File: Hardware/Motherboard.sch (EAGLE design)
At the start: 69 parts, among them J1 MICROMOD-2222-C, J10 MICRO-SD-PUSH-PUSH-EXT-PIN, J2 Vertical Qwiic Connector, J4 QWIIC_RIGHT_ANGLE, J5 CORTEX_JTAG_DEBUG_MINIMUM_PTH, J6 MICROMOD_CARRIER, J7 MICROMOD_CARRIER, Q1 3.1A/30V/105mΩ, U2 MCP73831, U5 AP7361C-33

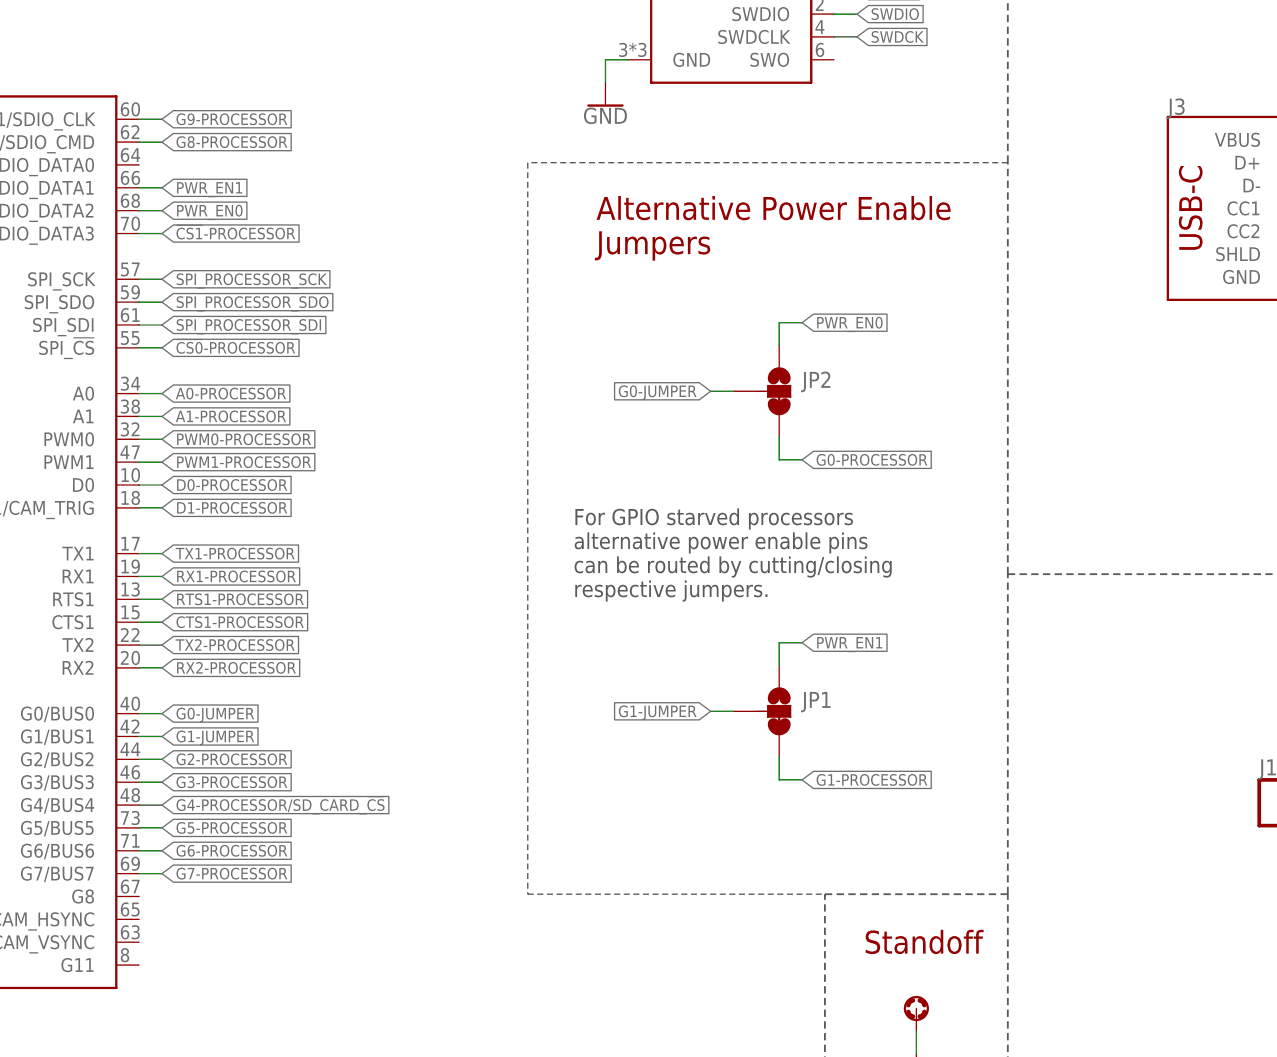
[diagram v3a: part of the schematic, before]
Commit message: Recreates changes from last change but instead moves jumpers to nets G5/G6
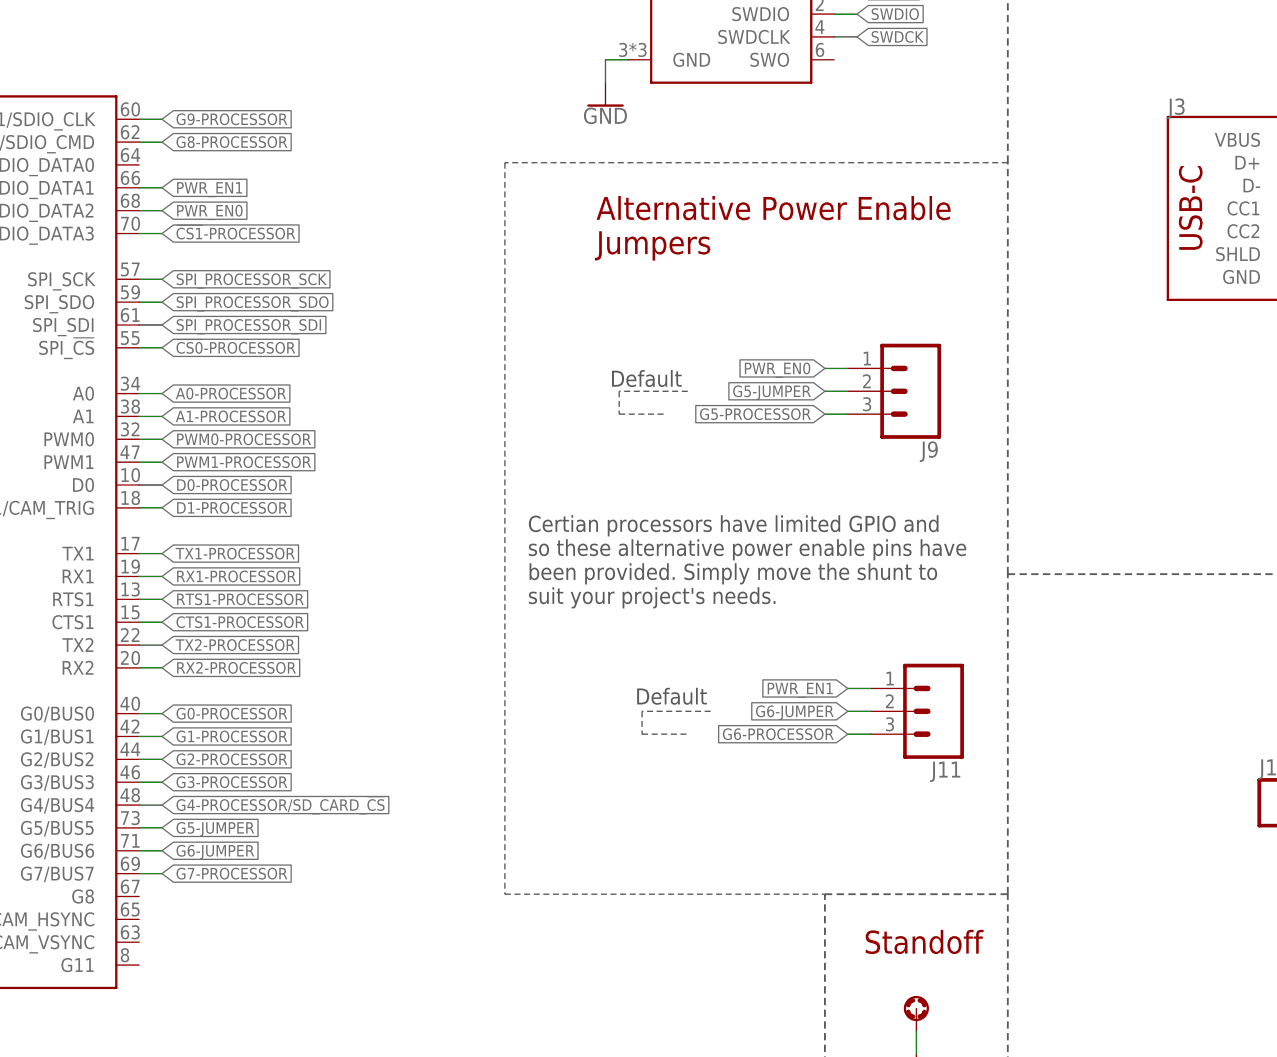
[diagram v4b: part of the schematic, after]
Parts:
- removed JP1, JP2: JUMPER-SMT_3_1-NC_TRACE_SILK, SparkFun-Jumpers:JUMPER-SMT_3_1-NC_TRACE_SILK
- added J11, J9: (no value), SparkFun-Connectors:CONN_03LOCK
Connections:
- removed net G0-JUMPER: J1.G0/BUS0, JP2.2
- removed net G1-JUMPER: J1.G1/BUS1, JP1.2
- new net G5-JUMPER: J1.G5/BUS5, J9.2
- new net G6-JUMPER: J1.G6/BUS6, J11.2
- net G0-PROCESSOR: now also J1.G0/BUS0; no longer JP2.3
- net G1-PROCESSOR: now also J1.G1/BUS1; no longer JP1.3
- net G5-PROCESSOR: now also J9.3; no longer J1.G5/BUS5
- net G6-PROCESSOR: now also J11.3; no longer J1.G6/BUS6
- net PWR_EN0: now also J9.1; no longer JP2.1
- net PWR_EN1: now also J11.1; no longer JP1.1
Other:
- note added: "Certian processors have limited GPIO and so these alternative power enable pins have been provided. Simply move the shunt to suit your project's needs."
- note added: "Default"
- note removed: "For GPIO starved processors alternative power enable pins can be routed by cutting/closing respective jumpers."
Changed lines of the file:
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@@
 <part name="R6" library="SparkFun-Resistors" deviceset="10KOHM" device="-0603-1/10W-1%" value="10k"/>
 <part name="GND8" library="SparkFun-PowerSymbols" deviceset="GND" device=""/>
-<part name="JP1" library="SparkFun-Jumpers" deviceset="JUMPER-SMT_3_1-NC_TRACE" device="_SILK" package3d_urn="urn:adsk.eagle:package:39288/1"/>
-<part name="JP2" library="SparkFun-Jumpers" deviceset="JUMPER-SMT_3_1-NC_TRACE" device="_SILK" package3d_urn="urn:adsk.eagle:package:39288/1"/>
+<part name="J9" library="SparkFun-Connectors" deviceset="CONN_03" device="LOCK"/>
+<part name="J11" library="SparkFun-Connectors" deviceset="CONN_03" device="LOCK"/>
 </parts>
 <sheets>
@@
 <text x="171.958" y="153.416" size="2.54" layer="94" font="vector">Standoff</text>
 <text x="187.96" y="22.86" size="2.54" layer="94" font="vector">Standoff</text>
-<wire x1="187.96" y1="241.3" x2="134.62" y2="241.3" width="0.1524" layer="97" style="longdash"/>
-<wire x1="134.62" y1="241.3" x2="134.62" y2="160.02" width="0.1524" layer="97" style="longdash"/>
-<wire x1="134.62" y1="160.02" x2="167.64" y2="160.02" width="0.1524" layer="97" style="longdash"/>
+<wire x1="187.96" y1="241.3" x2="132.08" y2="241.3" width="0.1524" layer="97" style="longdash"/>
+<wire x1="132.08" y1="241.3" x2="132.08" y2="160.02" width="0.1524" layer="97" style="longdash"/>
+<wire x1="132.08" y1="160.02" x2="167.64" y2="160.02" width="0.1524" layer="97" style="longdash"/>
 <text x="142.24" y="231.14" size="2.54" layer="94" font="vector">Alternative Power Enable
 Jumpers</text>
-<text x="139.7" y="193.04" size="1.778" layer="97" font="vector">For GPIO starved processors
-alternative power enable pins
-can be routed by cutting/closing
-respective jumpers.</text>
+<text x="134.62" y="192.278" size="1.778" layer="97" font="vector">Certian processors have limited GPIO and
+so these alternative power enable pins have
+been provided. Simply move the shunt to
+suit your project's needs.
+</text>
+<wire x1="154.94" y1="180.34" x2="147.32" y2="180.34" width="0.1524" layer="97" style="dashdot"/>
+<wire x1="147.32" y1="180.34" x2="147.32" y2="177.8" width="0.1524" layer="97" style="dashdot"/>
+<wire x1="147.32" y1="177.8" x2="152.4" y2="177.8" width="0.1524" layer="97" style="dashdot"/>
+<wire x1="152.4" y1="215.9" x2="144.78" y2="215.9" width="0.1524" layer="97" style="dashdot"/>
+<wire x1="144.78" y1="215.9" x2="144.78" y2="213.36" width="0.1524" layer="97" style="dashdot"/>
+<wire x1="144.78" y1="213.36" x2="149.86" y2="213.36" width="0.1524" layer="97" style="dashdot"/>
+<text x="143.764" y="216.408" size="1.778" layer="97" font="vector">Default</text>
+<text x="146.558" y="181.102" size="1.778" layer="97" font="vector">Default</text>
 </plain>
 <instances>
@@
 <attribute name="VALUE" x="264.16" y="218.186" size="1.778" layer="96" font="vector" align="top-center"/>
 </instance>
-<instance part="JP1" gate="G$1" x="162.56" y="180.34" smashed="yes">
-<attribute name="NAME" x="165.1" y="180.721" size="1.778" layer="95" font="vector"/>
-</instance>
-<instance part="JP2" gate="G$1" x="162.56" y="215.9" smashed="yes">
-<attribute name="NAME" x="165.1" y="216.281" size="1.778" layer="95" font="vector"/>
+<instance part="J9" gate="J$1" x="177.8" y="215.9" smashed="yes" rot="R180">
+<attribute name="VALUE" x="180.34" y="223.266" size="1.778" layer="96" font="vector" rot="R180"/>
+<attribute name="NAME" x="180.34" y="210.312" size="1.778" layer="95" font="vector" rot="R180"/>
+</instance>
+<instance part="J11" gate="J$1" x="180.34" y="180.34" smashed="yes" rot="R180">
+<attribute name="VALUE" x="182.88" y="187.706" size="1.778" layer="96" font="vector" rot="R180"/>
+<attribute name="NAME" x="182.88" y="174.752" size="1.778" layer="95" font="vector" rot="R180"/>
 </instance>
 </instances>
@@
 </segment>
 <segment>
-<pinref part="JP2" gate="G$1" pin="1"/>
-<wire x1="162.56" y1="220.98" x2="162.56" y2="223.52" width="0.1524" layer="91"/>
-<wire x1="162.56" y1="223.52" x2="165.1" y2="223.52" width="0.1524" layer="91"/>
-<label x="165.1" y="223.52" size="1.27" layer="95" font="vector" xref="yes"/>
+<label x="167.64" y="218.44" size="1.27" layer="95" font="vector" rot="R180" xref="yes"/>
+<pinref part="J9" gate="J$1" pin="1"/>
+<wire x1="170.18" y1="218.44" x2="167.64" y2="218.44" width="0.1524" layer="91"/>
 </segment>
 </net>
@@
 </segment>
 <segment>
-<pinref part="JP1" gate="G$1" pin="1"/>
-<wire x1="162.56" y1="185.42" x2="162.56" y2="187.96" width="0.1524" layer="91"/>
-<wire x1="162.56" y1="187.96" x2="165.1" y2="187.96" width="0.1524" layer="91"/>
-<label x="165.1" y="187.96" size="1.27" layer="95" font="vector" xref="yes"/>
+<label x="170.18" y="182.88" size="1.27" layer="95" font="vector" rot="R180" xref="yes"/>
+<pinref part="J11" gate="J$1" pin="1"/>
+<wire x1="172.72" y1="182.88" x2="170.18" y2="182.88" width="0.1524" layer="91"/>
 </segment>
 </net>
@@
 </segment>
 <segment>
-<pinref part="JP2" gate="G$1" pin="3"/>
-<wire x1="162.56" y1="210.82" x2="162.56" y2="208.28" width="0.1524" layer="91"/>
-<wire x1="162.56" y1="208.28" x2="165.1" y2="208.28" width="0.1524" layer="91"/>
-<label x="165.1" y="208.28" size="1.27" layer="95" font="vector" xref="yes"/>
+<pinref part="J1" gate="J1" pin="G0/BUS0"/>
+<wire x1="93.98" y1="180.086" x2="91.44" y2="180.086" width="0.1524" layer="91"/>
+<label x="93.98" y="180.086" size="1.27" layer="95" font="vector" xref="yes"/>
 </segment>
 </net>
@@
 </segment>
 <segment>
-<pinref part="JP1" gate="G$1" pin="3"/>
-<wire x1="162.56" y1="175.26" x2="162.56" y2="172.72" width="0.1524" layer="91"/>
-<wire x1="162.56" y1="172.72" x2="165.1" y2="172.72" width="0.1524" layer="91"/>
-<label x="165.1" y="172.72" size="1.27" layer="95" font="vector" xref="yes"/>
+<pinref part="J1" gate="J1" pin="G1/BUS1"/>
+<wire x1="93.98" y1="177.546" x2="91.44" y2="177.546" width="0.1524" layer="91"/>
+<label x="93.98" y="177.546" size="1.27" layer="95" font="vector" xref="yes"/>
 </segment>
 </net>
@@
 <net name="G5-PROCESSOR" class="0">
 <segment>
-<pinref part="J1" gate="J1" pin="G5/BUS5"/>
-<wire x1="91.44" y1="167.386" x2="93.98" y2="167.386" width="0.1524" layer="91"/>
-<label x="93.98" y="167.386" size="1.27" layer="95" font="vector" xref="yes"/>
-</segment>
-<segment>
 <wire x1="157.988" y1="42.672" x2="160.528" y2="42.672" width="0.1524" layer="91"/>
 <label x="160.528" y="42.672" size="1.27" layer="95" font="vector" xref="yes"/>
 <pinref part="J7" gate="J1" pin="G3"/>
 </segment>
+<segment>
+<label x="167.64" y="213.36" size="1.27" layer="95" font="vector" rot="R180" xref="yes"/>
+<pinref part="J9" gate="J$1" pin="3"/>
+<wire x1="170.18" y1="213.36" x2="167.64" y2="213.36" width="0.1524" layer="91"/>
+</segment>
 </net>
 <net name="G6-PROCESSOR" class="0">
-<segment>
-<pinref part="J1" gate="J1" pin="G6/BUS6"/>
-<wire x1="91.44" y1="164.846" x2="93.98" y2="164.846" width="0.1524" layer="91"/>
-<label x="93.98" y="164.846" size="1.27" layer="95" font="vector" xref="yes"/>
-</segment>
 <segment>
 <wire x1="157.988" y1="40.132" x2="160.528" y2="40.132" width="0.1524" layer="91"/>
 <label x="160.528" y="40.132" size="1.27" layer="95" font="vector" xref="yes"/>
 <pinref part="J7" gate="J1" pin="G4"/>
+</segment>
+<segment>
+<label x="170.18" y="177.8" size="1.27" layer="95" font="vector" rot="R180" xref="yes"/>
+<pinref part="J11" gate="J$1" pin="3"/>
+<wire x1="172.72" y1="177.8" x2="170.18" y2="177.8" width="0.1524" layer="91"/>
 </segment>
 </net>
@@
 </segment>
 </net>
-<net name="G1-JUMPER" class="0">
-<segment>
-<pinref part="JP1" gate="G$1" pin="2"/>
-<wire x1="157.48" y1="180.34" x2="154.94" y2="180.34" width="0.1524" layer="91"/>
-<label x="154.94" y="180.34" size="1.27" layer="95" font="vector" rot="R180" xref="yes"/>
-</segment>
-<segment>
-<pinref part="J1" gate="J1" pin="G1/BUS1"/>
-<wire x1="93.98" y1="177.546" x2="91.44" y2="177.546" width="0.1524" layer="91"/>
-<label x="93.98" y="177.546" size="1.27" layer="95" font="vector" xref="yes"/>
-</segment>
-</net>
-<net name="G0-JUMPER" class="0">
-<segment>
-<pinref part="JP2" gate="G$1" pin="2"/>
-<wire x1="157.48" y1="215.9" x2="154.94" y2="215.9" width="0.1524" layer="91"/>
-<label x="154.94" y="215.9" size="1.27" layer="95" font="vector" rot="R180" xref="yes"/>
-</segment>
-<segment>
-<pinref part="J1" gate="J1" pin="G0/BUS0"/>
-<wire x1="93.98" y1="180.086" x2="91.44" y2="180.086" width="0.1524" layer="91"/>
-<label x="93.98" y="180.086" size="1.27" layer="95" font="vector" xref="yes"/>
-</segment>
-</net>
+<net name="G5-JUMPER" class="0">
+<segment>
+<label x="167.64" y="215.9" size="1.27" layer="95" font="vector" rot="R180" xref="yes"/>
+<pinref part="J9" gate="J$1" pin="2"/>
+<wire x1="170.18" y1="215.9" x2="167.64" y2="215.9" width="0.1524" layer="91"/>
+</segment>
+<segment>
+<pinref part="J1" gate="J1" pin="G5/BUS5"/>
+<wire x1="91.44" y1="167.386" x2="93.98" y2="167.386" width="0.1524" layer="91"/>
+<label x="93.98" y="167.386" size="1.27" layer="95" font="vector" xref="yes"/>
+</segment>
+</net>
+<net name="G6-JUMPER" class="0">
+<segment>
+<label x="170.18" y="180.34" size="1.27" layer="95" font="vector" rot="R180" xref="yes"/>
+<pinref part="J11" gate="J$1" pin="2"/>
+<wire x1="172.72" y1="180.34" x2="170.18" y2="180.34" width="0.1524" layer="91"/>
+</segment>
+<segment>
+<pinref part="J1" gate="J1" pin="G6/BUS6"/>
+<wire x1="91.44" y1="164.846" x2="93.98" y2="164.846" width="0.1524" layer="91"/>
+<label x="93.98" y="164.846" size="1.27" layer="95" font="vector" xref="yes"/>
+</segment>
+</net>

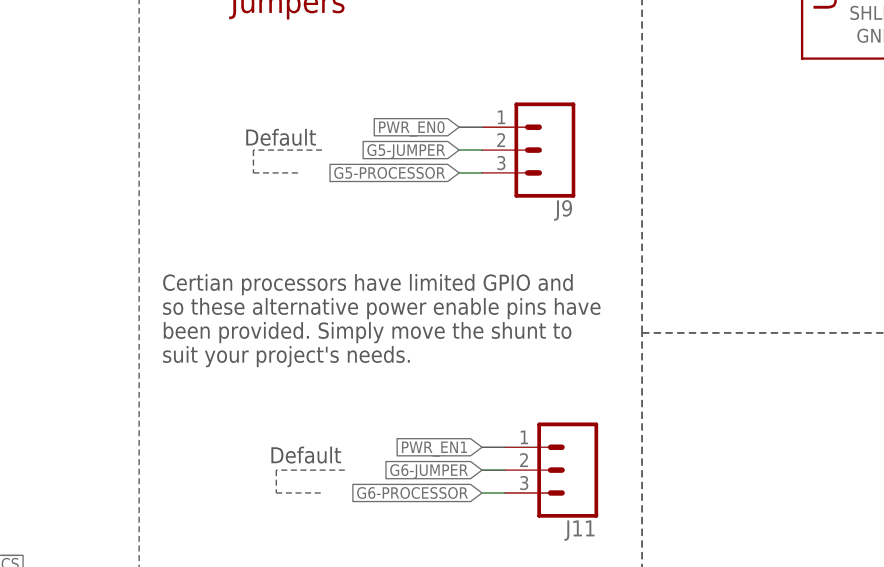
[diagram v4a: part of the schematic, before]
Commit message: Fixes typo
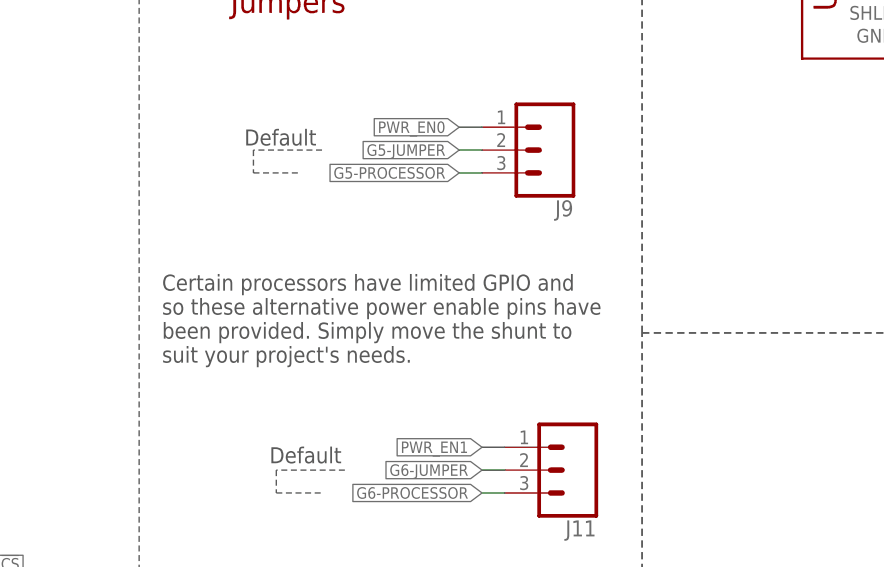
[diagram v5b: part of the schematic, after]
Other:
- note added: "Certain processors have limited GPIO and so these alternative power enable pins have been provided. Simply move the shunt to suit your project's needs."
- note removed: "Certian processors have limited GPIO and so these alternative power enable pins have been provided. Simply move the shunt to suit your project's needs."
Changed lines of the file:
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@@
 <text x="142.24" y="231.14" size="2.54" layer="94" font="vector">Alternative Power Enable
 Jumpers</text>
-<text x="134.62" y="192.278" size="1.778" layer="97" font="vector">Certian processors have limited GPIO and
+<text x="134.62" y="192.278" size="1.778" layer="97" font="vector">Certain processors have limited GPIO and
 so these alternative power enable pins have
 been provided. Simply move the shunt to
